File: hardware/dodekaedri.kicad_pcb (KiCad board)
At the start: 4 copper layers, 76.2 x 76.2 mm, 227 parts, among them CON401 BARREL_JACK, J801 HANDSFREE, P301 BNC, P801 TX_SW_WIRE, P802 USB_OTG, P803 UART, P804 PROG, P805 RNG_PINS, P806 CONN_01X08, P807 CONN_01X04, P808 CONN_02X04, P809 BOOT0JMPR, Q501 BCP56, Q502 IRL510, Q801 BSS84, SW801 SW_PUSH, SW802 SW, SW803 SW, SW804 SW, SW806 encoder, SW807 RESET, T301 TRANSFO, T302 TRANSFO, T501 TRANSFO2, T601 TRANSFO2, U201 MIC5365, U202 SI5351A, U401 NCP3170-D, U501 74LVC1G3157, U502 74LVC1G3157, U601 74LVC1G3157, U602 74LVC1G3157, U603 TL972IDR, U701 WM8731, U702 MCP6L02, U801 STM32F401, U802 WM8731

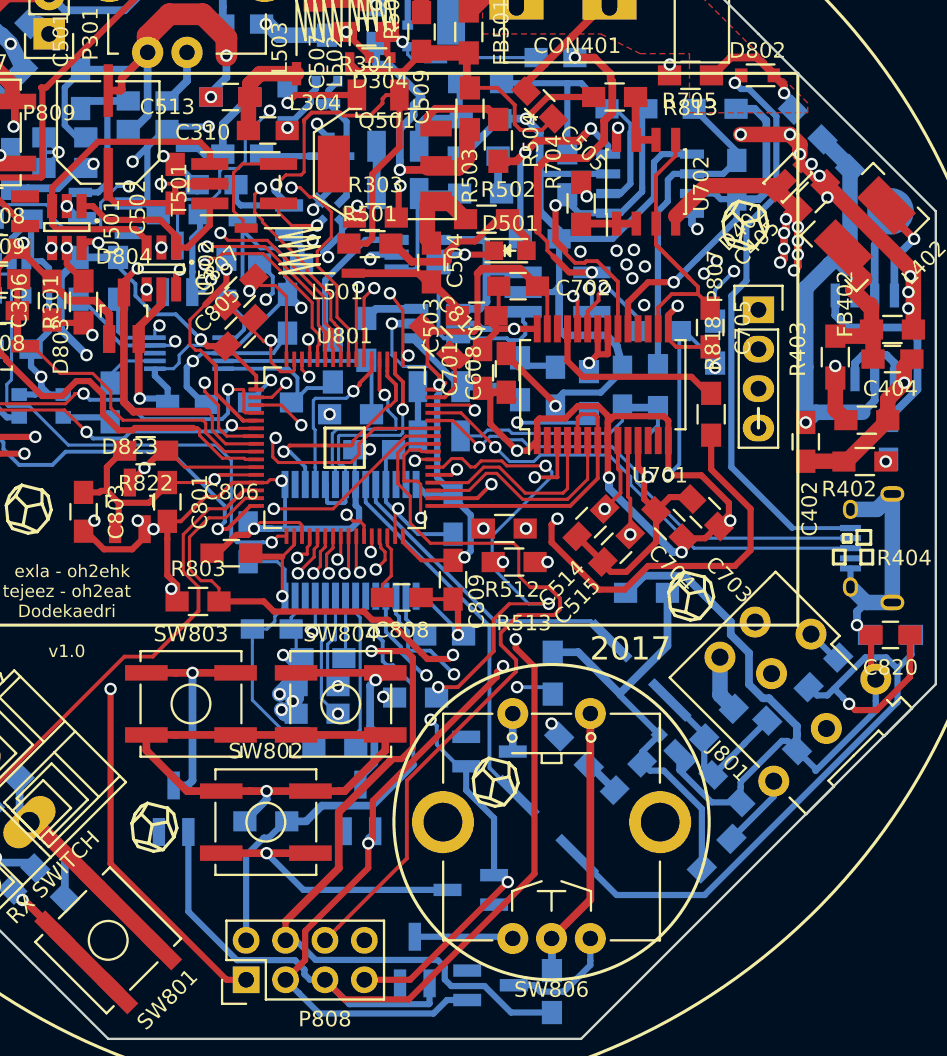
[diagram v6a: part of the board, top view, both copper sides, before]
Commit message: Added M2.5 mounting holes
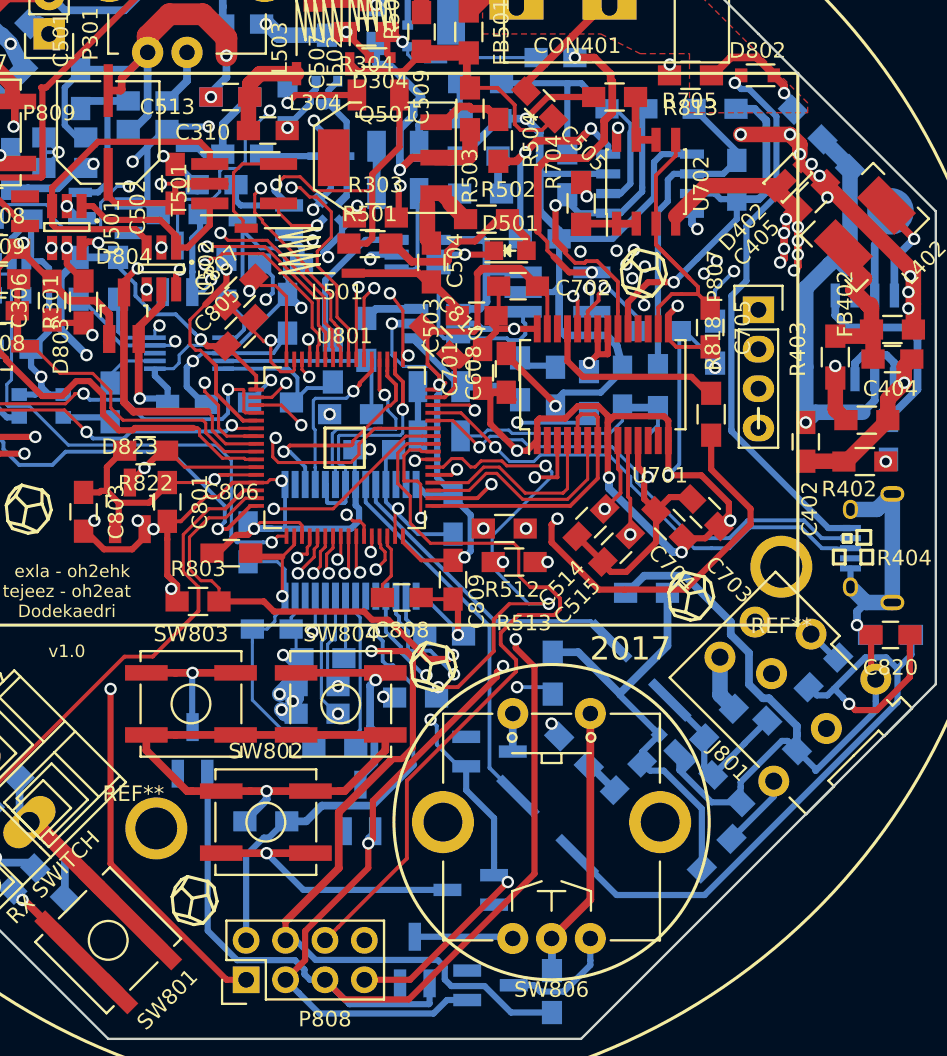
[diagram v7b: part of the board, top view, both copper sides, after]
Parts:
- added REF**: m2.5_mounting_hole_small, dodekaedri:m2.5_mounting_hole_small, F.Cu at (171.7, 92.8)
- added REF**: m2.5_mounting_hole_small, dodekaedri:m2.5_mounting_hole_small, F.Cu at (131.4, 109.6)
- moved D806 3.95 mm to (133.7, 104.6)
- moved Q501 0.41 mm to (146.1, 66.4)
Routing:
- net /CPU/RX_TX: track 31.0 -> 25.2 mm
- net Net-(D806-Pad1): track 14.3 -> 10.0 mm
- net /CPU/UI_SW_GRID2: track 130.9 -> 134.1 mm
- net Net-(D802-Pad2): track 37.8 -> 36.5 mm
- net Net-(Q501-Pad3): track 6.08 -> 4.77 mm
- net /CPU/PA12/USB: track 31.2 -> 32.3 mm
- net Net-(C306-Pad1): track 48.0 -> 49.1 mm
- net Net-(R818-Pad1): track 34.8 -> 33.8 mm
- net /CPU/PA11/USB: track 31.0 -> 32.0 mm
- net Net-(C504-Pad2): track 5.55 -> 6.15 mm

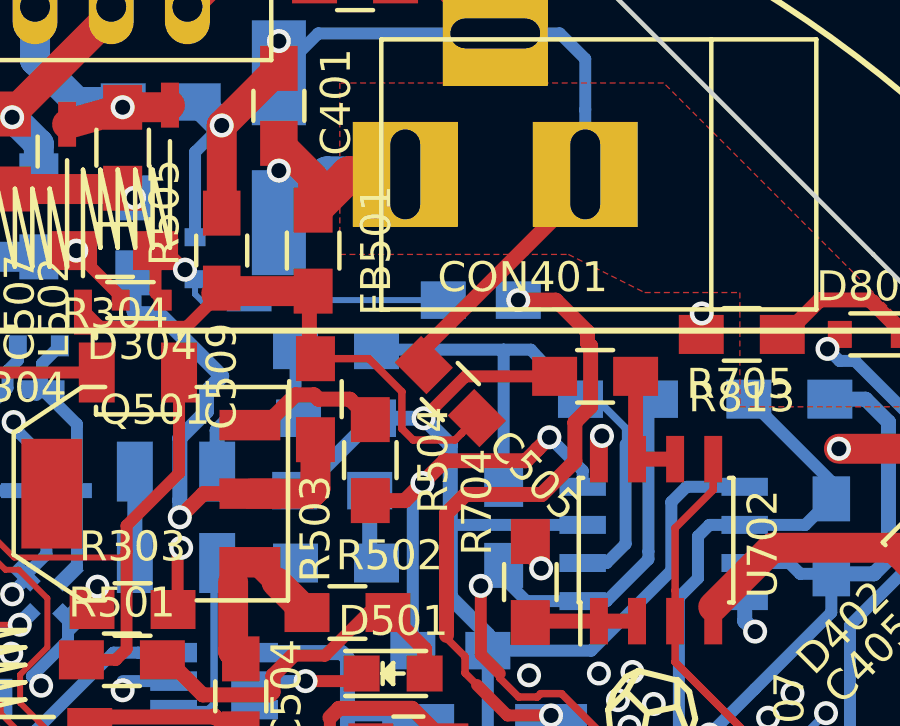
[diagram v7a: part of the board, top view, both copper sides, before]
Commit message: changed some component values
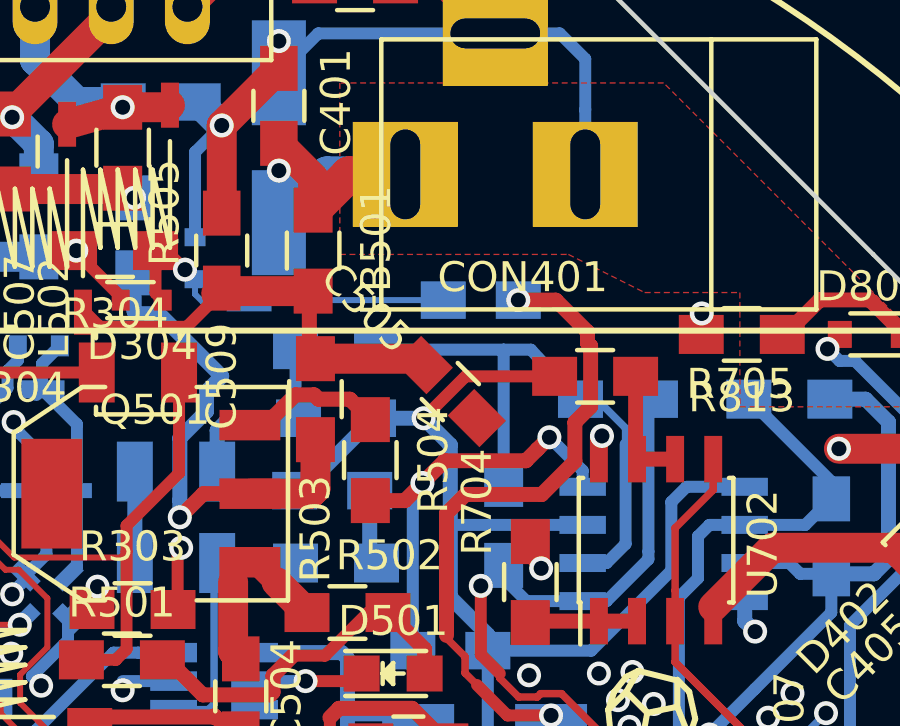
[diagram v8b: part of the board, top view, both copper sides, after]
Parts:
- turned C505 to 315 degrees
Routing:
- net GND: track 519.3 -> 511.1 mm
- net Net-(C505-Pad1): track 18.7 -> 14.7 mm
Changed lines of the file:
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@@
     (thickness 1.6)
     (drawings 302)
-    (tracks 3116)
+    (tracks 3110)
     (zones 0)
     (modules 229)
@@
   (layers
     (0 F.Cu signal)
-    (1 In1.Cu mixed)
+    (1 In1.Cu mixed hide)
     (2 In2.Cu jumper)
     (31 B.Cu signal)
@@
   )
   (setup
-    (last_trace_width 0.2)
+    (last_trace_width 1)
     (user_trace_width 0.2)
     (user_trace_width 0.25)
@@
   )
   (module Capacitors_SMD:C_0805_HandSoldering (layer F.Cu)
-    (at 156.083 62.992 135)
+    (at 156.083 62.992 315)
     (descr "Capacitor SMD 0805, hand soldering")
     (tags "capacitor 0805")
     (attr smd)
-    (fp_text reference C505 (at -3.951313 0 135) (layer F.SilkS)
+    (fp_text reference C505 (at -3.951313 0 315) (layer F.SilkS)
       (effects (font (size 1 1) (thickness 0.15)))
     )
-    (fp_text value 100nF (at 0 2.1 135) (layer F.Fab)
+    (fp_text value 100nF (at 0 2.1 315) (layer F.Fab)
       (effects (font (size 1 1) (thickness 0.15)))
     )
@@
     (fp_line (start 0.5 -0.85) (end -0.5 -0.85) (layer F.SilkS) (width 0.15))
     (fp_line (start -0.5 0.85) (end 0.5 0.85) (layer F.SilkS) (width 0.15))
-    (pad 1 smd rect (at -1.25 0 135) (size 1.5 1.25) (layers F.Cu F.Paste F.Mask)
+    (pad 1 smd rect (at -1.25 0 315) (size 1.5 1.25) (layers F.Cu F.Paste F.Mask)
       (net 24 "Net-(C505-Pad1)"))
-    (pad 2 smd rect (at 1.25 0 135) (size 1.5 1.25) (layers F.Cu F.Paste F.Mask)
+    (pad 2 smd rect (at 1.25 0 315) (size 1.5 1.25) (layers F.Cu F.Paste F.Mask)
       (net 2 GND))
     (model Capacitors_SMD.3dshapes/C_0805_HandSoldering.wrl
@@
   (segment (start 158.985001 64.915999) (end 159.385 64.516) (width 0.5) (layer F.Cu) (net 2))
   (segment (start 153.416 66.628) (end 153.463 66.628) (width 0.5) (layer F.Cu) (net 2))
-  (segment (start 154.795 61.976) (end 160.58134 56.18966) (width 0.5) (layer F.Cu) (net 2))
   (segment (start 160.58134 56.18966) (end 160.58134 55.753) (width 0.5) (layer F.Cu) (net 2))
   (segment (start 176.403 80.678) (end 176.403 79.629) (width 0.5) (layer B.Cu) (net 2))
@@
   (segment (start 148.844 71.648) (end 149.098 71.902) (width 1) (layer F.Cu) (net 23))
   (segment (start 150.288 69.342) (end 151.304 70.358) (width 1) (layer F.Cu) (net 23))
-  (segment (start 151.384 61.896) (end 153.369002 61.896) (width 0.25) (layer F.Cu) (net 24))
-  (segment (start 154.845999 64.606001) (end 156.236765 64.606001) (width 0.25) (layer F.Cu) (net 24))
-  (segment (start 153.369002 61.896) (end 154.468999 62.995997) (width 0.25) (layer F.Cu) (net 24))
-  (segment (start 154.468999 62.995997) (end 154.468999 64.229001) (width 0.25) (layer F.Cu) (net 24))
-  (segment (start 154.468999 64.229001) (end 154.845999 64.606001) (width 0.25) (layer F.Cu) (net 24))
-  (segment (start 156.236765 64.606001) (end 156.454231 64.388535) (width 0.25) (layer F.Cu) (net 24))
-  (segment (start 156.454231 64.388535) (end 156.966883 63.875883) (width 0.25) (layer F.Cu) (net 24))
+  (segment (start 151.5872 61.896) (end 154.987 61.896) (width 1) (layer F.Cu) (net 24))
+  (segment (start 154.987 61.896) (end 155.199117 62.108117) (width 1) (layer F.Cu) (net 24))
   (segment (start 144.399 60.833) (end 147.298 60.833) (width 0.4) (layer F.Cu) (net 24))
   (segment (start 147.298 60.833) (end 148.463 59.668) (width 0.4) (layer F.Cu) (net 24))
